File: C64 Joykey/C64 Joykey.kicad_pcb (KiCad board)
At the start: 2 copper layers, 99.7 x 74.9 mm, 24 parts, among them J1 Port_1, J2 Port_2, M1 Mounting, M2 Mounting, M3 Mounting, M4 Mounting, SW1 FIRE1, SW2 FIRE2, SW3 FIRE3, SW4 UP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

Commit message: Routed tracks
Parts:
- added JP4: DEFAULT_FW, Pin_Headers:Pin_Header_Straight_1x02_Pitch2.54mm, F.Cu at (191.1, 121.9)
- added REF***: KiCad-Logo2_6mm_SilkScreen, Symbols:KiCad-Logo2_6mm_SilkScreen, F.Cu at (219.7, 118.7)
- added REF***: OSHW-Logo2_9.8x8mm_SilkScreen, Symbols:OSHW-Logo2_9.8x8mm_SilkScreen, F.Cu at (219.7, 111.1)
- J1, J2: footprint Connector_IDC:IDC-Header_2x05_P2.54mm_Vertical -> C64 IDC:IDC_Joystick
- moved R1 0.64 mm to (200.0, 100.3)
- moved R2 0.64 mm to (200.0, 104.1)
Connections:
- A1 pad 10: P2_FIRE2 -> /FIRE3_POL
- A1 pad 11: P2_FIRE3 -> Net-(A1-Pad11)
- A1 pad 13: (no net) -> P2_LEFT
- A1 pad 14: (no net) -> P2_DOWN
- A1 pad 15: (no net) -> P2_RIGHT
- A1 pad 16: (no net) -> P2_UP
- A1 pad 5: P2_UP -> /FIRE1_IN
- A1 pad 6: P2_DOWN -> P2_FIRE2
- A1 pad 7: P2_LEFT -> /FIRE3_IN
- A1 pad 8: P2_RIGHT -> P2_FIRE1
- A1 pad 9: P2_FIRE1 -> /FIRE2_POL
- JP3 pad 2: Net-(JP3-Pad2) -> /FIRE3_IN
- R1 pad 1: Net-(R1-Pad1) -> /FIRE2_POL
- R2 pad 1: Net-(R2-Pad1) -> /FIRE3_POL
- SW1 pad 1: P2_FIRE1 -> /FIRE1_IN
- SW2 pad 2: Net-(R1-Pad1) -> /FIRE2_POL
- SW3 pad 1: Net-(JP3-Pad2) -> /FIRE3_IN
- SW3 pad 2: Net-(R2-Pad1) -> /FIRE3_POL
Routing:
- net /FIRE3_IN: track 0.00 -> 115.3 mm, vias 0 -> 3
- net P2_FIRE1: track 2.54 -> 115.0 mm, vias 0 -> 4
- net VCC: track 0.00 -> 112.0 mm
- net P2_FIRE2: track 2.54 -> 109.2 mm, vias 0 -> 2
- net P2_DOWN: track 2.54 -> 103.4 mm, vias 0 -> 2
- net Net-(D2-Pad2): track 0.00 -> 99.5 mm
- net Net-(D1-Pad2): track 0.00 -> 90.0 mm
- net P2_LEFT: track 2.54 -> 88.9 mm, vias 0 -> 3
- net P2_RIGHT: track 2.54 -> 85.8 mm, vias 0 -> 1
- net /FIRE1_IN: track 0.00 -> 81.5 mm, vias 0 -> 4
- net /FIRE3_POL: track 0.00 -> 78.4 mm, vias 0 -> 1
- net P1_FIRE1: track 0.00 -> 77.8 mm
- net /FIRE2_POL: track 0.00 -> 61.5 mm
- net P2_UP: track 2.54 -> 63.7 mm, vias 0 -> 1
- net Net-(A1-Pad22): track 6.50 -> 45.7 mm
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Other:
- outline, holes or cut-outs redrawn
- net class PWR added: clearance 0.2, trace_width 0.381, via_dia 0.8, via_drill 0.4
- board text added: "C64 JoyKey github.com/tebl"
- board text added: "Configure FIRE2/FIRE3 polarity must be set to what system expects. VCC C64/VIC-20 GND Amiga/Atari ST/SMS N/C Unsupported system"
- board text added: "Default FW (fire1 wired)"
- board text added: "FIRE2 POLARITY"
- board text added: "FIRE3 OUTPUT"
- board text added: "FIRE3 POLARITY"
- board text added: "GND"
- board text added: "Licensed under CERN OHL v1.2"
- board text added: "P1 FIRE1"
- board text added: "P2 FIRE3"
- board text added: "PORT 1"
- board text added: "PORT 2"
- board text added: "PWR"
- board text added: "SYS"
- board text added: "VCC"

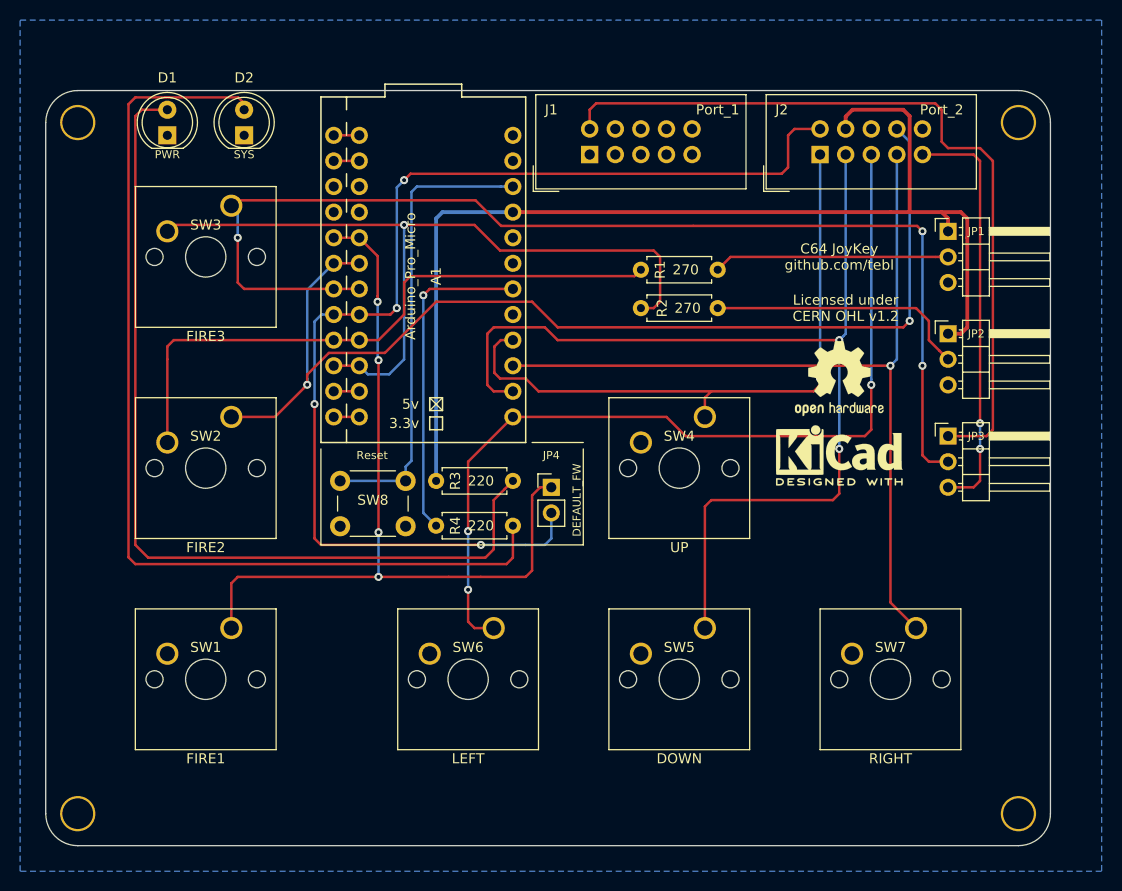
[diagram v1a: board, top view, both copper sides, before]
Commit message: Tweaked PCB layout
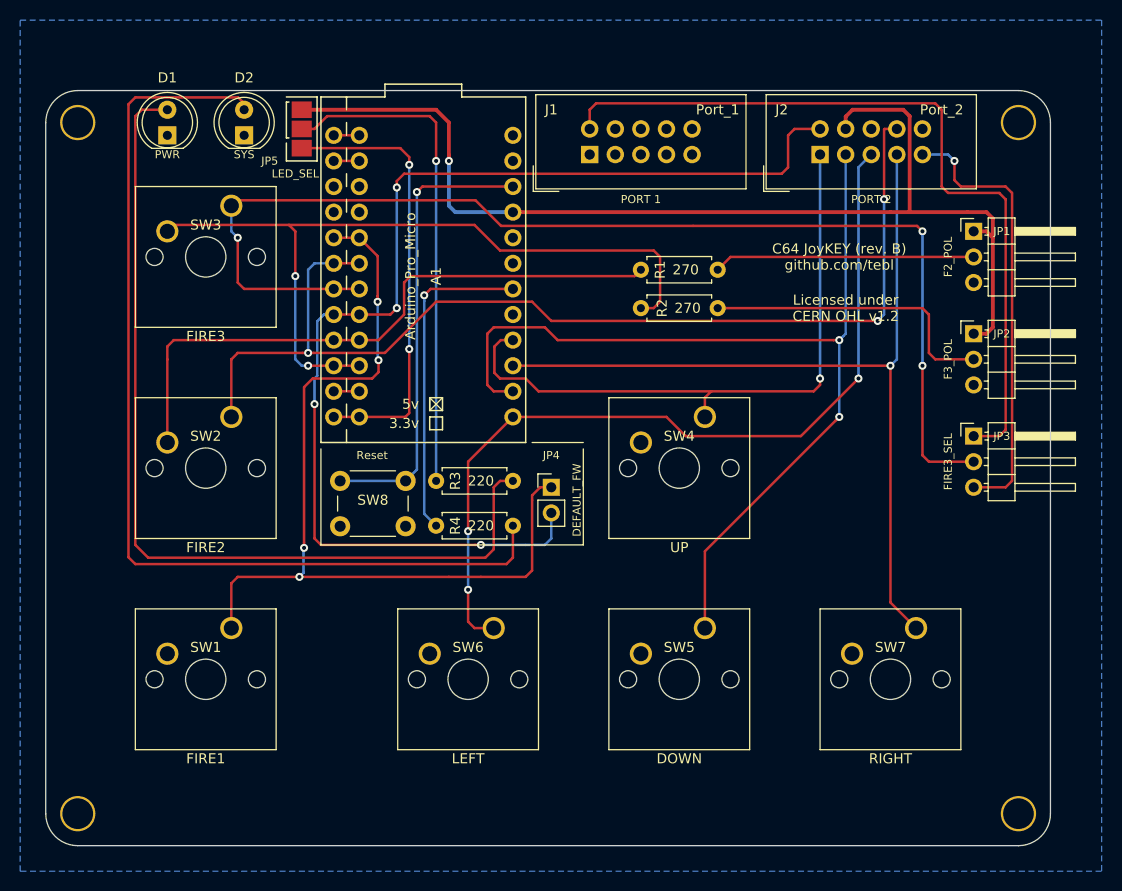
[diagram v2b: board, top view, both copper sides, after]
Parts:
- removed REF***: KiCad-Logo2_6mm_SilkScreen, Symbols:KiCad-Logo2_6mm_SilkScreen
- removed REF***: OSHW-Logo2_9.8x8mm_SilkScreen, Symbols:OSHW-Logo2_9.8x8mm_SilkScreen
- added JP5: LED_SEL, solder_bridge:select, F.Cu at (166.4, 84.5)
- JP1: value F2_COM -> F2_POL
- JP2: value F3_COM -> F3_POL
- moved JP1 2.54 mm to (233.0, 96.5)
- moved JP2 2.54 mm to (233.0, 106.7)
- moved JP3 2.54 mm to (233.0, 116.8)
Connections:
- R3 pad 1: VCC -> Net-(JP5-Pad2)
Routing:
- net Net-(JP5-Pad2): track 0.00 -> 49.7 mm, vias 0 -> 1
- net Net-(A1-Pad12): track 2.54 -> 44.1 mm, vias 0 -> 2
- net P2_DOWN: track 103.4 -> 96.4 mm
- net /FIRE1_IN: track 81.5 -> 88.2 mm
- net P2_LEFT: track 88.9 -> 85.2 mm
- net Net-(JP2-Pad2): track 26.1 -> 29.7 mm
- net P2_FIRE3: track 41.2 -> 44.2 mm, vias 2 -> 1
- net Net-(JP1-Pad2): track 23.4 -> 25.9 mm
- net /FIRE3_IN: track 115.3 -> 117.9 mm
- net P2_FIRE2: track 109.2 -> 107.2 mm, vias 2 -> 3
- net VCC: track 112.0 -> 110.7 mm, vias 0 -> 1
- net /FIRE3_POL: track 78.4 -> 77.3 mm, vias 1 -> 2
- net Net-(D1-Pad2): track 90.0 -> 90.7 mm
- net Net-(A1-Pad22): track 45.7 -> 45.4 mm, vias 0 -> 1
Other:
- board text added: "1"
- board text added: "2"
- board text added: "3"
- board text added: "C64 JoyKEY (rev. B) github.com/tebl"
- board text added: "Configure FIRE2/FIRE3 polarity must be set to what system expects. VCC C64/VIC-20 GND Amiga/USB/SMS N/C Unsupported system"
- board text added: "Install Arduino Pro Micro, if needed for USB function. Hold down LEFT + RIGHT key on powerup to enable. FIRE2/3 polarity must be set to GND to use enable use of these keys over USB."
- board text added: "PWR SELECT (2-3 for Arduino)"
- board text removed: "C64 JoyKey github.com/tebl"
- board text removed: "Configure FIRE2/FIRE3 polarity must be set to what system expects. VCC C64/VIC-20 GND Amiga/Atari ST/SMS N/C Unsupported system"

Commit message: Added polarity notes
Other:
- board text added: "POLARITY C64 Amiga Atari Atari_ST SMS Kempston P2 FIRE2 VCC GND N/C GND GND GND P2 FIRE3 VCC GND N/C GND N/C GND"
- board text added: "~IMPORTANT! Configure FIRE2/FIRE3 polarity according to what the system supports, or left unjumpered (N/C) just to be safe. Risk of harm to your system if not done correctly."
- board text removed: "Configure FIRE2/FIRE3 polarity must be set to what system expects. VCC C64/VIC-20 GND Amiga/USB/SMS N/C Unsupported system"
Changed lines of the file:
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@@
   (general
     (thickness 1.6)
-    (drawings 126)
+    (drawings 127)
     (tracks 289)
     (zones 0)
@@
   (page A4)
   (layers
-    (0 F.Cu signal)
-    (31 B.Cu signal)
+    (0 F.Cu signal hide)
+    (31 B.Cu signal hide)
     (32 B.Adhes user)
     (33 F.Adhes user)
@@
     )
   )
+  (gr_text "POLARITY  C64 Amiga Atari Atari_ST SMS Kempston\nP2 FIRE2  VCC GND   N/C GND     GND GND\nP2 FIRE3  VCC GND   N/C GND     N/C GND" (at 210.82 154.305) (layer B.SilkS)
+    (effects (font (size 1 1) (thickness 0.15)) (justify left mirror))
+  )
   (gr_text "PORT 2" (at 222.885 93.345) (layer F.SilkS)
     (effects (font (size 0.8 0.8) (thickness 0.1)))
@@
   (gr_line (start 167.894 89.662) (end 167.894 83.058) (layer B.SilkS) (width 0.12))
   (gr_line (start 164.592 83.058) (end 167.894 83.058) (layer B.SilkS) (width 0.12))
-  (gr_text "Configure FIRE2/FIRE3\npolarity must be set to\nwhat system expects.\n\nVCC C64/VIC-20\nGND Amiga/USB/SMS\nN/C Unsupported system" (at 227.965 104.14) (layer B.SilkS)
-    (effects (font (size 1 1) (thickness 0.15)) (justify left mirror))
+  (gr_text "~IMPORTANT!\nConfigure FIRE2/FIRE3 polarity according to what the\nsystem supports, or left unjumpered (N/C) just to be safe.\nRisk of harm to your system if not done correctly." (at 193.675 146.685) (layer B.SilkS)
+    (effects (font (size 1 1) (thickness 0.15)) (justify mirror))
   )
   (gr_text "Licensed under\nCERN OHL v1.2" (at 220.345 104.14) (layer F.SilkS)

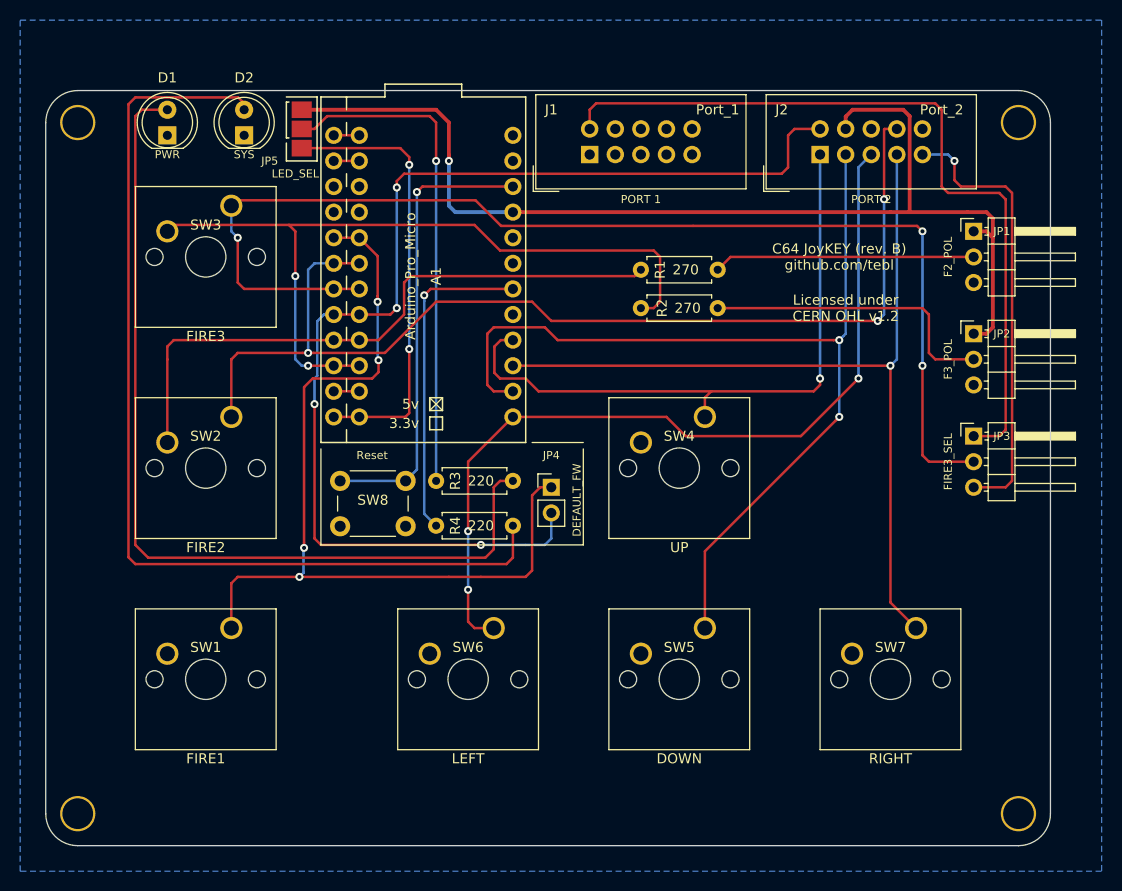
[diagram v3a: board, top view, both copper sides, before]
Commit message: Added second DEFAULT_FW so all buttons can be independent
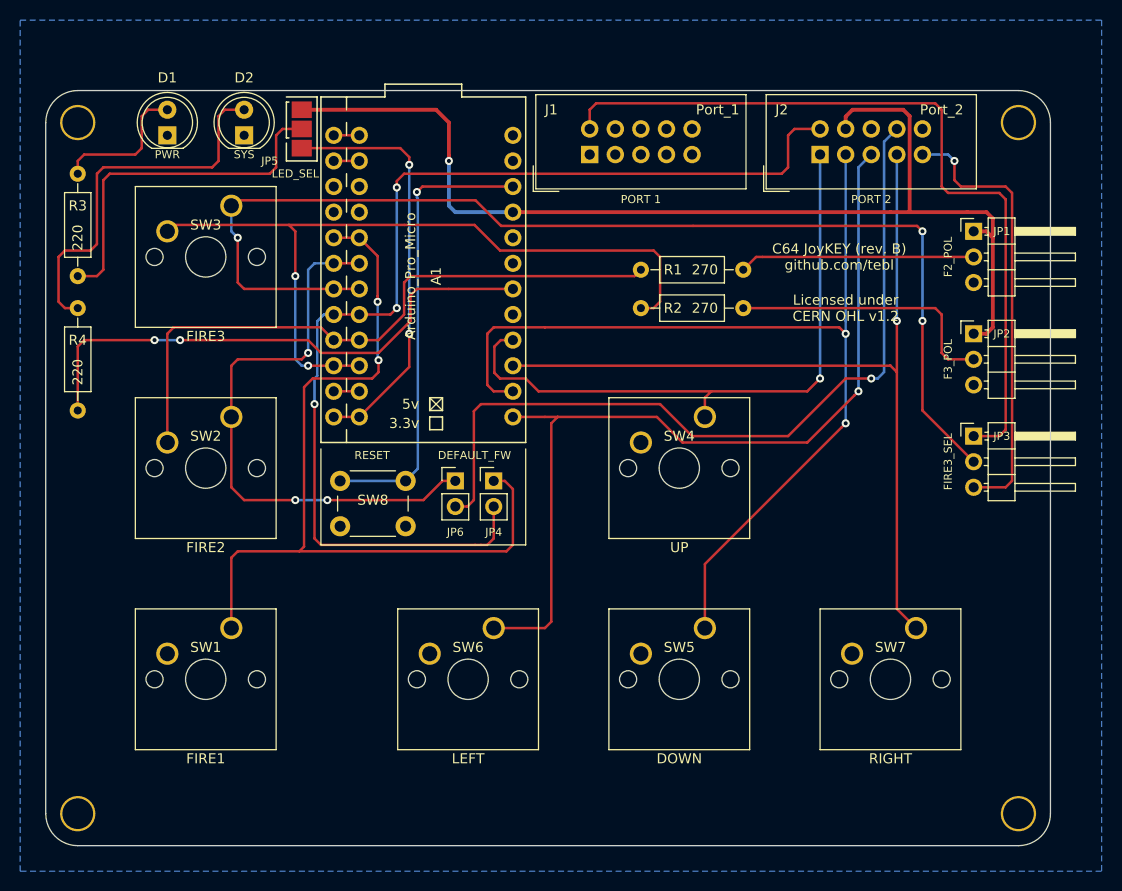
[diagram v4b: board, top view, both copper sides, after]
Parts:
- added JP6: DEFAULT_FW, Pin_Headers:Pin_Header_Straight_1x02_Pitch2.54mm, F.Cu at (181.6, 121.3)
- R1, R2, R3, R4: footprint Resistors_THT:R_Axial_DIN0207_L6.3mm_D2.5mm_P7.62mm_Horizontal -> Resistors_THT:R_Axial_DIN0207_L6.3mm_D2.5mm_P10.16mm_Horizontal
- SW8: value Reset -> RESET
- moved R3 46.8 mm to (144.1, 90.8), turned to 270 degrees
- moved R4 41.6 mm to (144.1, 104.1), turned to 270 degrees
- moved JP4 5.75 mm to (185.4, 121.3)
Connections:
- A1 pad 6: P2_FIRE2 -> /FIRE2_IN
- R3 pad 1: Net-(JP5-Pad2) -> Net-(D1-Pad2)
- R3 pad 2: Net-(D1-Pad2) -> Net-(JP5-Pad2)
- R4 pad 1: Net-(A1-Pad18) -> Net-(D2-Pad2)
- R4 pad 2: Net-(D2-Pad2) -> Net-(A1-Pad18)
- SW2 pad 1: P2_FIRE2 -> /FIRE2_IN
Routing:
- net Net-(D1-Pad2): track 90.7 -> 14.1 mm
- net Net-(D2-Pad2): track 99.5 -> 37.8 mm
- net /FIRE2_IN: track 0.00 -> 57.3 mm, vias 0 -> 3
- net P2_FIRE2: track 107.2 -> 80.5 mm, vias 3 -> 1
- net Net-(A1-Pad18): track 32.4 -> 54.4 mm, vias 1 -> 2
- net Net-(JP5-Pad2): track 49.7 -> 35.3 mm, vias 1 -> 0
- net P2_FIRE1: track 115.3 -> 110.2 mm, vias 4 -> 3
- net /FIRE1_IN: track 88.2 -> 84.4 mm, vias 4 -> 2
- net P2_LEFT: track 85.2 -> 88.0 mm, vias 3 -> 1
- net Net-(A1-Pad12): track 44.1 -> 41.4 mm
- net /FIRE3_IN: track 117.9 -> 115.3 mm
- net Net-(JP1-Pad2): track 25.9 -> 23.4 mm
- net Net-(JP2-Pad2): track 29.7 -> 27.2 mm
- net /FIRE2_POL: track 61.5 -> 63.3 mm
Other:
- board text added: "Default FW (FIRE1/FIRE2 wired directly)"
- board text added: "Install Arduino Pro Micro, if needed for USB function. Hold down LEFT + RIGHT key on powerup to enable. FIRE2/3 polarity must be set to GND, keys will be disabled USB-mode if not."
- board text removed: "Default FW (fire1 wired)"
- board text removed: "Install Arduino Pro Micro, if needed for USB function. Hold down LEFT + RIGHT key on powerup to enable. FIRE2/3 polarity must be set to GND to use enable use of these keys over USB."

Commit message: Added protection diodes
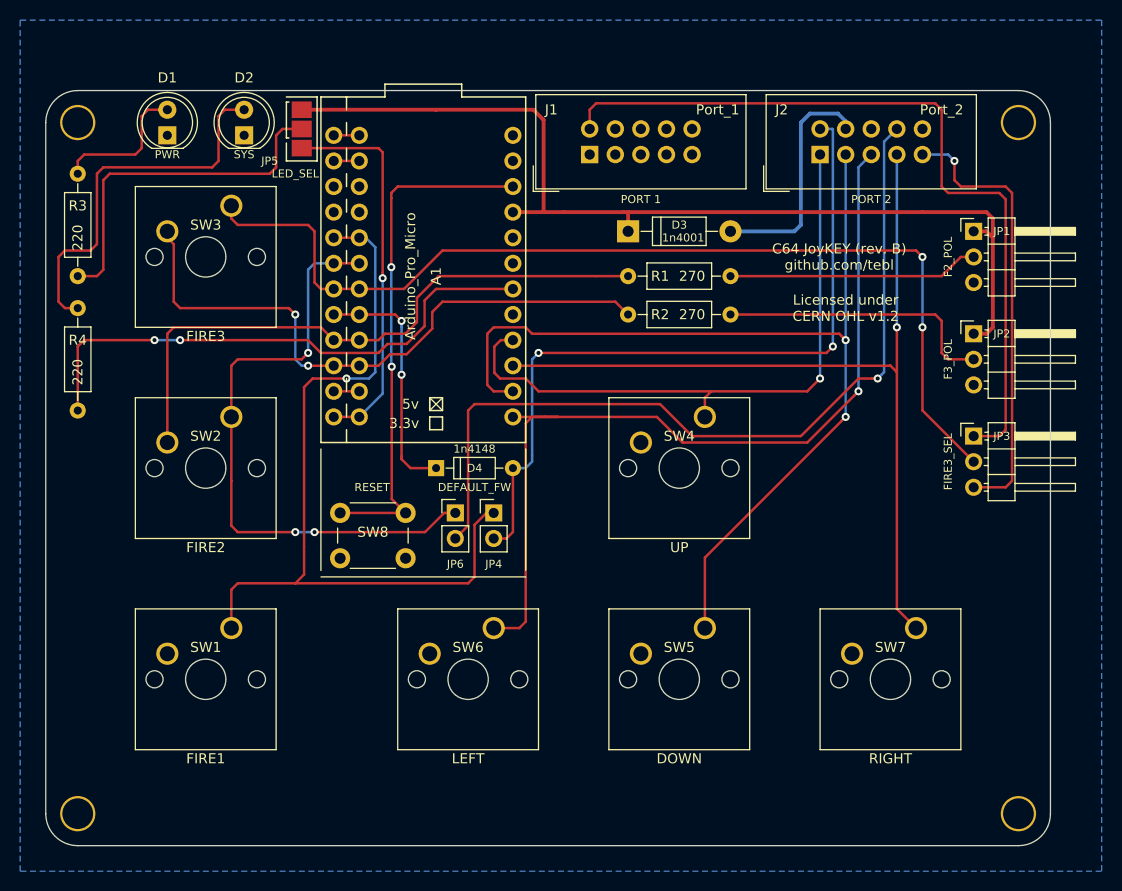
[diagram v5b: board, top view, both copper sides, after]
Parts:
- added D3: 1n4001, Diodes_THT:D_DO-41_SOD81_P10.16mm_Horizontal, F.Cu at (198.8, 96.5)
- added D4: 1n4148, Diodes_THT:D_DO-35_SOD27_P7.62mm_Horizontal, F.Cu at (179.7, 120.0)
- moved JP4 3.17 mm to (185.4, 124.5)
- moved JP6 3.17 mm to (181.6, 124.5)
- moved SW8 3.17 mm to (170.2, 124.5)
- moved R1 1.42 mm to (198.8, 101.0)
- moved R2 1.42 mm to (198.8, 104.8)
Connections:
- A1 pad 8: P2_FIRE1 -> /FIRE1_OUT
- J2 pad 7: VCC -> Net-(D3-Pad2)
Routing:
- net P2_FIRE1: track 110.2 -> 74.0 mm, vias 3 -> 2
- net /FIRE1_OUT: track 0.00 -> 24.5 mm, vias 0 -> 2
- net Net-(D3-Pad2): track 0.00 -> 23.3 mm
- net /FIRE3_POL: track 77.3 -> 61.7 mm
- net /FIRE3_IN: track 115.3 -> 100.0 mm, vias 3 -> 2
- net VCC: track 110.7 -> 98.5 mm, vias 1 -> 0
- net Net-(A1-Pad22): track 45.5 -> 51.2 mm, vias 1 -> 2
- net /FIRE1_IN: track 84.4 -> 80.4 mm, vias 2 -> 1
- net /FIRE2_IN: track 57.3 -> 60.9 mm
- net Net-(A1-Pad12): track 41.4 -> 38.0 mm, vias 2 -> 1
- net P2_FIRE2: track 80.5 -> 83.4 mm
- net /FIRE2_POL: track 63.3 -> 61.3 mm
- net Net-(JP1-Pad2): track 23.4 -> 24.9 mm
- net Net-(JP2-Pad2): track 27.2 -> 27.8 mm
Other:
- board text added: "Amiga GND GND"
- board text added: "Atari N/C N/C"
- board text added: "Atari_ST GND GND"
- board text added: "C64 VCC VCC"
- board text added: "Default FW (FIRE1/FIRE2)"
- board text added: "Kempston GND GND"
- board text added: "POLARITY P2 FIRE2 P2 FIRE3"
- board text added: "SMS GND N/C"
- board text added: "USB GND GND"
- board text removed: "Default FW (FIRE1/FIRE2 wired directly)"
- board text removed: "POLARITY C64 Amiga Atari Atari_ST SMS Kempston P2 FIRE2 VCC GND N/C GND GND GND P2 FIRE3 VCC GND N/C GND N/C GND"
